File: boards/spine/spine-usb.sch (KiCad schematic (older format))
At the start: 34 parts, among them P1 USB_B, U1 93C56, U2 FT2232H, Y1 12 MHz

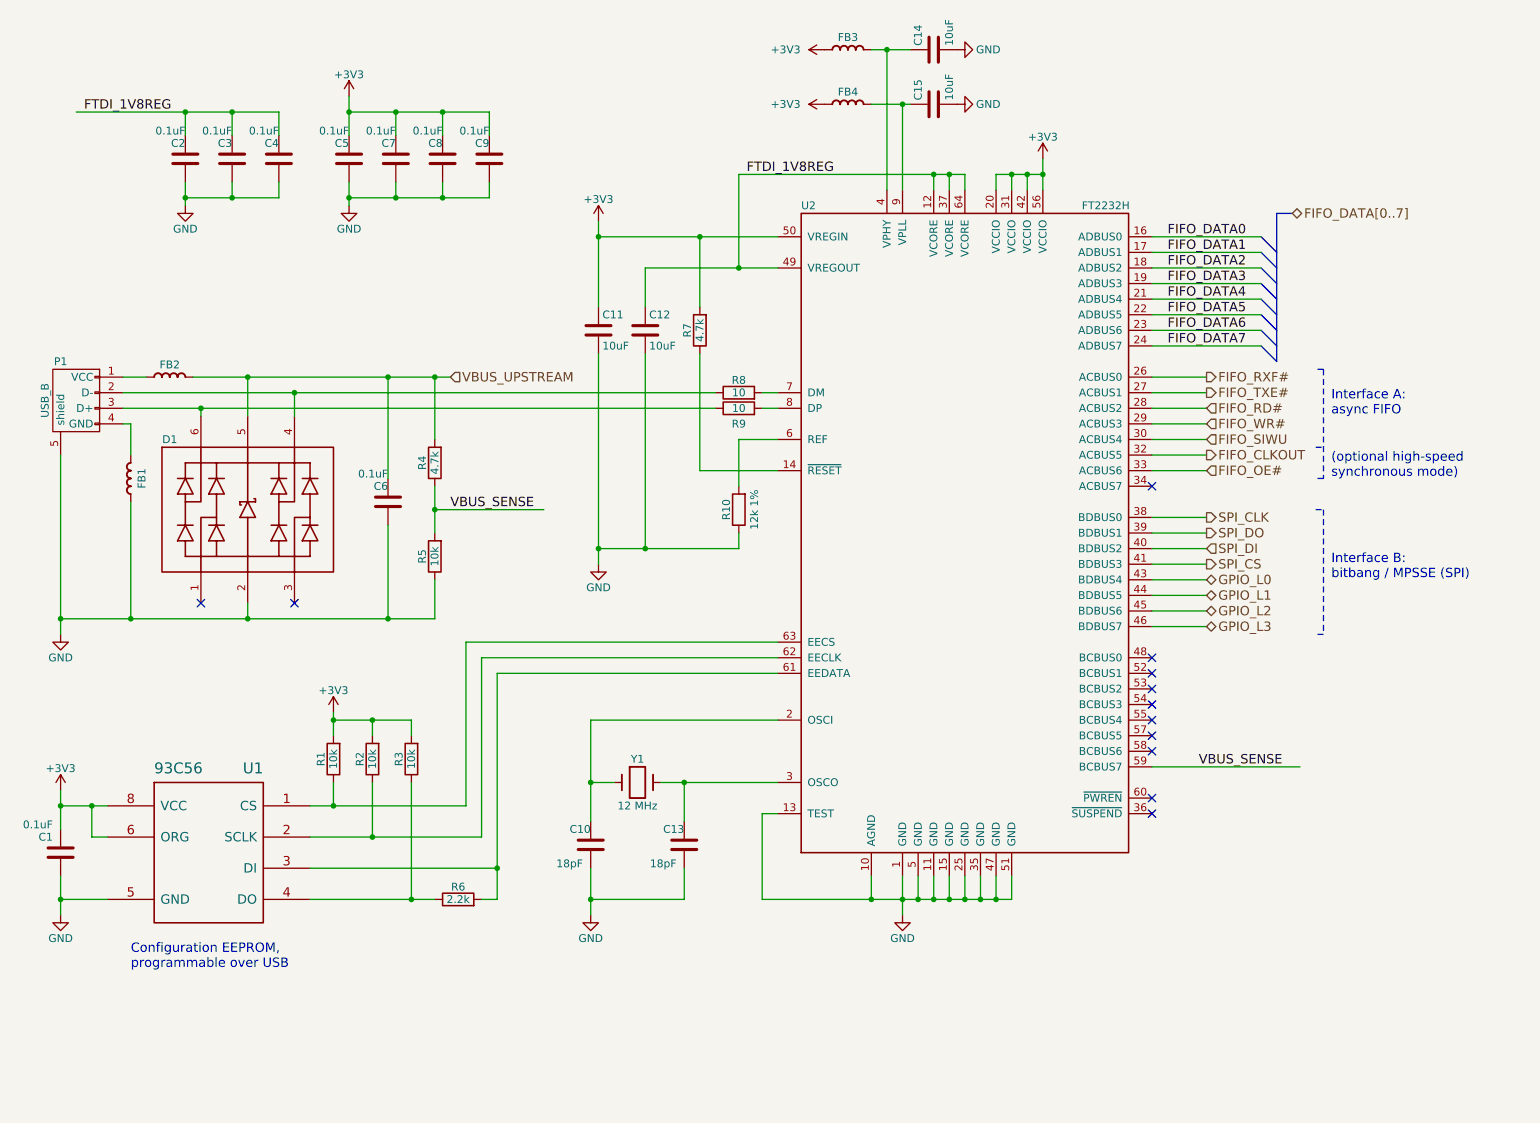
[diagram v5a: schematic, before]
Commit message: Pick better capacitors :)
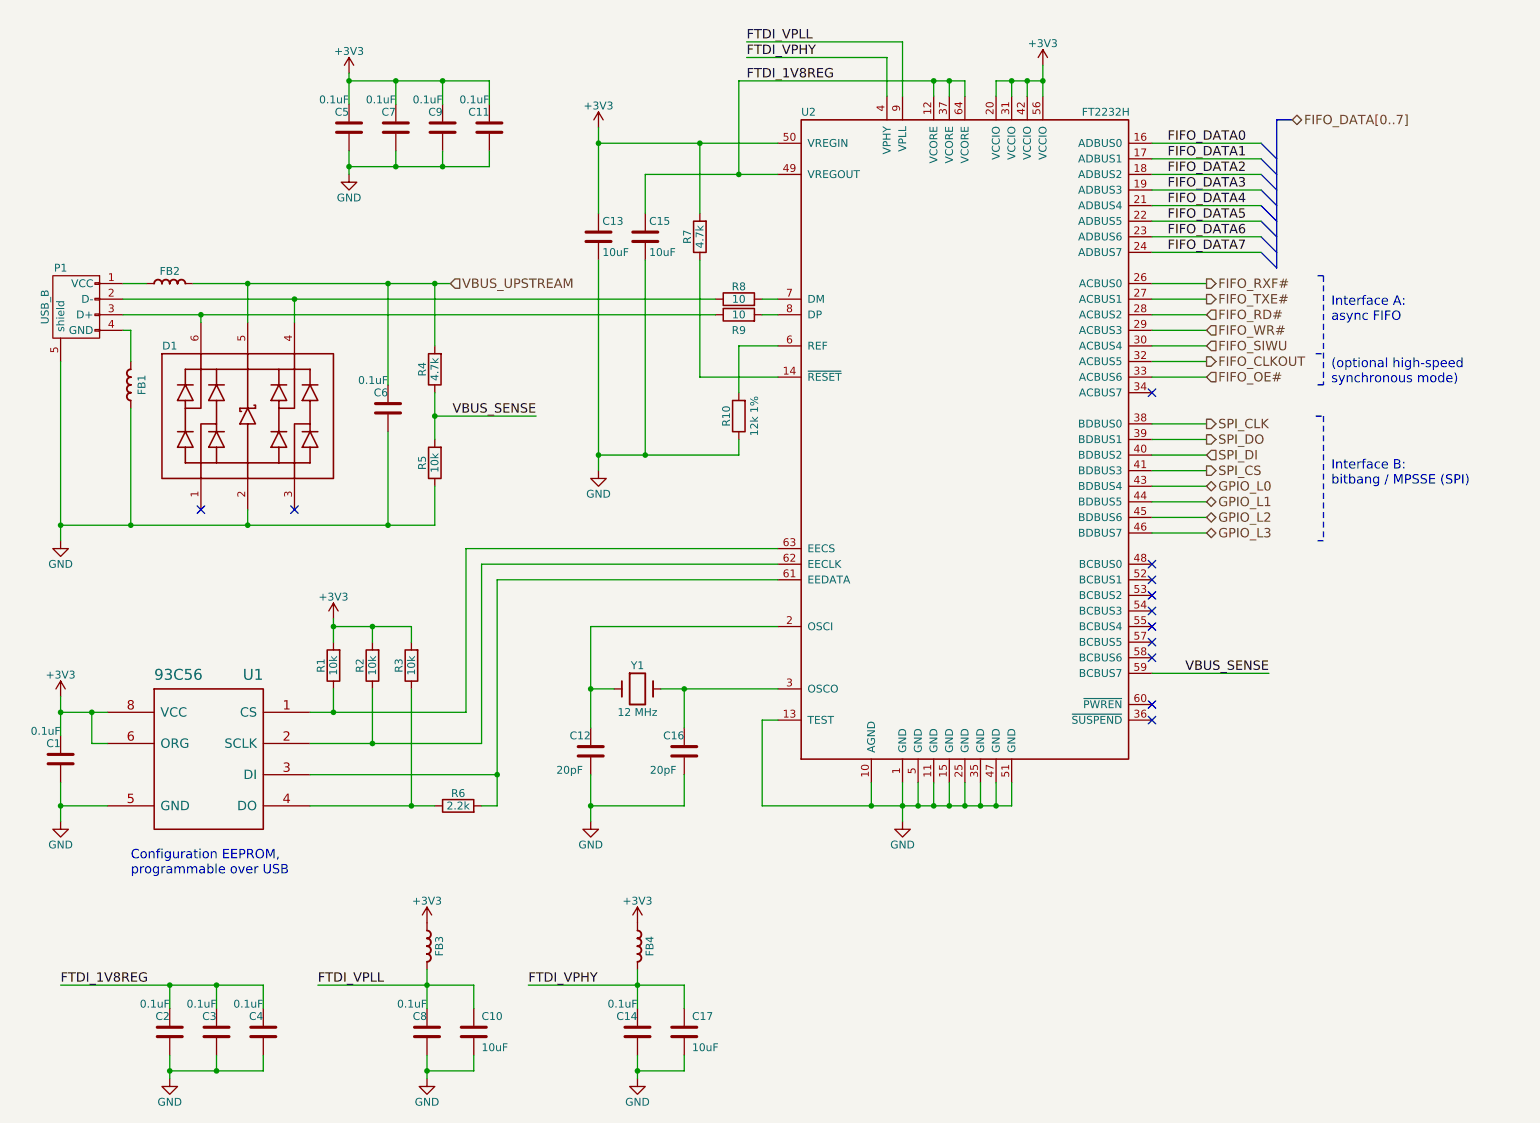
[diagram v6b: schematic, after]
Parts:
- removed C12: 10uF, symbol C
- removed C13: 18pF, symbol C
- removed FB3: Ferrite bead, symbol FERRITE_BEAD
- added C10, C17: 10uF, 1206, symbol C
- added C11: 0.1uF, 0805, symbol C
- added C16: 20pF, 0805, symbol C
- added FB4: Ferrite bead, symbol FERRITE_BEAD
- C1, C2, C3, C4, C5, C6, C7, C8, C9: footprint (none) -> 0805; MfgId CC0805ZRY5V9BB104 -> GRM21BR71H104MA01L; MfrId Yageo -> Murata; RefPrice1k 0.00783 -> 0.01880; Vend1Id 311-1361-1-ND -> 490-9672-2-ND
- C12: renamed from C10; value 18pF -> 20pF; footprint (none) -> 0805; MfgId CC0805JRNPO9BN180 -> CL21C200JBANNNC; MfrId Yageo -> Samsung; RefPrice1k 0.01266 -> 0.01485; Vend1Id 311-1102-1-ND -> 1276-1829-1-ND
- C13: renamed from C11; footprint (none) -> 1206; MfgId CC0805ZKY5V6BB106 -> GRM31CR61H106MA12L; MfrId Yageo -> Murata; RefPrice1k 0.03080 -> 0.07429; Vend1Id 311-1355-1-ND -> 490-10756-2-ND
- C14: value 10uF -> 0.1uF; footprint (none) -> 0805; MfgId CC0805ZKY5V6BB106 -> GRM21BR71H104MA01L; MfrId Yageo -> Murata; RefPrice1k 0.03080 -> 0.01880; Vend1Id 311-1355-1-ND -> 490-9672-2-ND
- C15: footprint (none) -> 1206; MfgId CC0805ZKY5V6BB106 -> GRM31CR61H106MA12L; MfrId Yageo -> Murata; RefPrice1k 0.03080 -> 0.07429; Vend1Id 311-1355-1-ND -> 490-10756-2-ND
- renumbered FB4 to FB3
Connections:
- net labels added: FTDI_VPHY, FTDI_VPLL
- wire segments 134 -> 146
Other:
- moved on the sheet: C12, C13, C2, D1, FB1, FB2, FB3, P1, R1, R10, R2, R3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

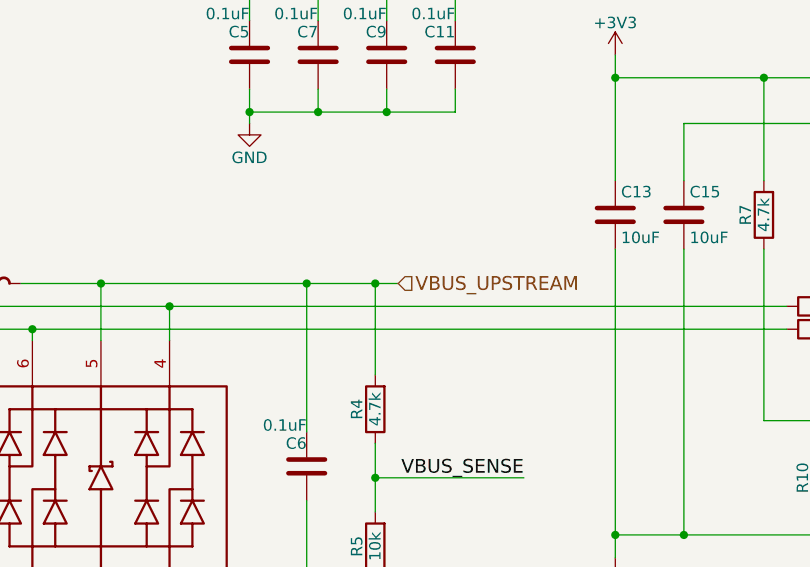
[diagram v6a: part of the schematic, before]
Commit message: Early power management work
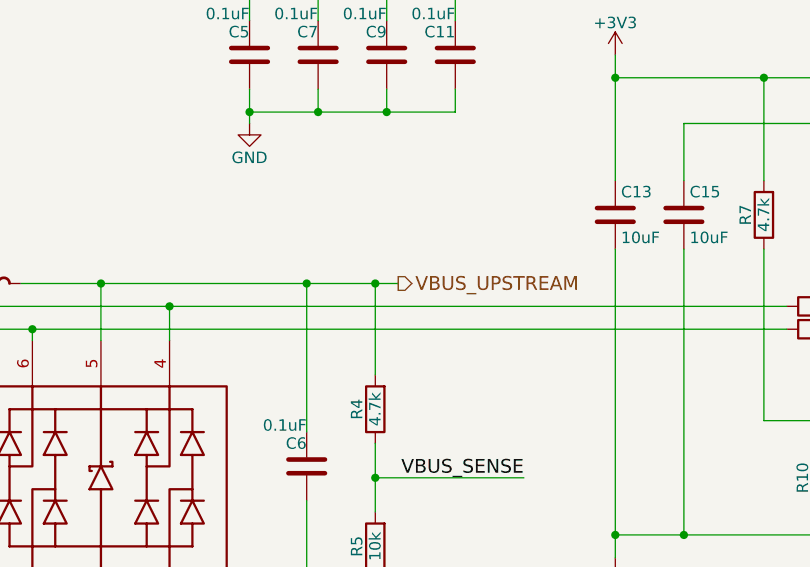
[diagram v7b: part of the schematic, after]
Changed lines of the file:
@@
 $Descr USLetter 11000 8500
 encoding utf-8
-Sheet 2 5
+Sheet 2 6
 Title ""
 Date ""
@@
 	1    0    0    -1
 $EndComp
-Text HLabel 3550 2350 2    60   Input ~ 0
+Text HLabel 3550 2350 2    60   Output ~ 0
 VBUS_UPSTREAM
 Text Label 4100 3200 2    60   ~ 0
@@
 $EndComp
 $Comp
-L GND #PWR01
+L GND #PWR1
 U 1 1 563F3C00
 P 1050 4000
-F 0 "#PWR01" H 1050 3750 50  0001 C CNN
+F 0 "#PWR1" H 1050 3750 50  0001 C CNN
 F 1 "GND" H 1050 3850 50  0000 C CNN
 F 2 "" H 1050 4000 60  0000 C CNN
@@
 $EndComp
 $Comp
-L +3V3 #PWR02
+L +3V3 #PWR11
 U 1 1 563F5B33
 P 4500 1350
-F 0 "#PWR02" H 4500 1200 50  0001 C CNN
+F 0 "#PWR11" H 4500 1200 50  0001 C CNN
 F 1 "+3V3" H 4500 1490 50  0000 C CNN
 F 2 "" H 4500 1350 60  0000 C CNN
@@
 NoConn ~ 1950 3800
 $Comp
-L GND #PWR03
+L GND #PWR12
 U 1 1 56407FC9
 P 4500 3550
-F 0 "#PWR03" H 4500 3300 50  0001 C CNN
+F 0 "#PWR12" H 4500 3300 50  0001 C CNN
 F 1 "GND" H 4500 3400 50  0000 C CNN
 F 2 "" H 4500 3550 60  0000 C CNN
@@
 $EndComp
 $Comp
-L +3V3 #PWR04
+L +3V3 #PWR16
 U 1 1 56409B2C
 P 7350 950
-F 0 "#PWR04" H 7350 800 50  0001 C CNN
+F 0 "#PWR16" H 7350 800 50  0001 C CNN
 F 1 "+3V3" H 7350 1090 50  0000 C CNN
 F 2 "" H 7350 950 60  0000 C CNN
@@
 $EndComp
 $Comp
-L +3V3 #PWR05
+L +3V3 #PWR2
 U 1 1 5640C498
 P 1050 5000
-F 0 "#PWR05" H 1050 4850 50  0001 C CNN
+F 0 "#PWR2" H 1050 4850 50  0001 C CNN
 F 1 "+3V3" H 1050 5140 50  0000 C CNN
 F 2 "" H 1050 5000 60  0000 C CNN
@@
 $EndComp
 $Comp
-L GND #PWR06
+L GND #PWR3
 U 1 1 5640C700
 P 1050 5800
-F 0 "#PWR06" H 1050 5550 50  0001 C CNN
+F 0 "#PWR3" H 1050 5550 50  0001 C CNN
 F 1 "GND" H 1050 5650 50  0000 C CNN
 F 2 "" H 1050 5800 60  0000 C CNN
@@
 $EndComp
 $Comp
-L +3V3 #PWR07
+L +3V3 #PWR5
 U 1 1 5640CB0D
 P 2800 4500
-F 0 "#PWR07" H 2800 4350 50  0001 C CNN
+F 0 "#PWR5" H 2800 4350 50  0001 C CNN
 F 1 "+3V3" H 2800 4640 50  0000 C CNN
 F 2 "" H 2800 4500 60  0000 C CNN
@@
 $EndComp
 $Comp
-L GND #PWR08
+L GND #PWR4
 U 1 1 5640EC58
 P 1750 7450
-F 0 "#PWR08" H 1750 7200 50  0001 C CNN
+F 0 "#PWR4" H 1750 7200 50  0001 C CNN
 F 1 "GND" H 1750 7300 50  0000 C CNN
 F 2 "" H 1750 7450 60  0000 C CNN
@@
 $EndComp
 $Comp
-L GND #PWR09
+L GND #PWR7
 U 1 1 5640ECEA
 P 2900 1650
-F 0 "#PWR09" H 2900 1400 50  0001 C CNN
+F 0 "#PWR7" H 2900 1400 50  0001 C CNN
 F 1 "GND" H 2900 1500 50  0000 C CNN
 F 2 "" H 2900 1650 60  0000 C CNN
@@
 FTDI_1V8REG
 $Comp
-L +3V3 #PWR010
+L +3V3 #PWR6
 U 1 1 5640F443
 P 2900 1000
-F 0 "#PWR010" H 2900 850 50  0001 C CNN
+F 0 "#PWR6" H 2900 850 50  0001 C CNN
 F 1 "+3V3" H 2900 1140 50  0000 C CNN
 F 2 "" H 2900 1000 60  0000 C CNN
@@
 $EndComp
 $Comp
-L GND #PWR011
+L GND #PWR10
 U 1 1 56411C34
 P 4450 5800
-F 0 "#PWR011" H 4450 5550 50  0001 C CNN
+F 0 "#PWR10" H 4450 5550 50  0001 C CNN
 F 1 "GND" H 4450 5650 50  0000 C CNN
 F 2 "" H 4450 5800 60  0000 C CNN
@@
 $EndComp
 $Comp
-L GND #PWR012
+L GND #PWR15
 U 1 1 56412014
 P 6450 5800
-F 0 "#PWR012" H 6450 5550 50  0001 C CNN
+F 0 "#PWR15" H 6450 5550 50  0001 C CNN
 F 1 "GND" H 6450 5650 50  0000 C CNN
 F 2 "" H 6450 5800 60  0000 C CNN
@@
 $EndComp
 $Comp
-L GND #PWR013
+L GND #PWR9
 U 1 1 5642A93B
 P 3400 7450
-F 0 "#PWR013" H 3400 7200 50  0001 C CNN
+F 0 "#PWR9" H 3400 7200 50  0001 C CNN
 F 1 "GND" H 3400 7300 50  0000 C CNN
 F 2 "" H 3400 7450 60  0000 C CNN
@@
 	3700 7400 3700 7300
 $Comp
-L +3V3 #PWR014
+L +3V3 #PWR8
 U 1 1 5642B955
 P 3400 6450
-F 0 "#PWR014" H 3400 6300 50  0001 C CNN
+F 0 "#PWR8" H 3400 6300 50  0001 C CNN
 F 1 "+3V3" H 3400 6590 50  0000 C CNN
 F 2 "" H 3400 6450 60  0000 C CNN
@@
 $EndComp
 $Comp
-L GND #PWR015
+L GND #PWR14
 U 1 1 5642BC5C
 P 4750 7450
-F 0 "#PWR015" H 4750 7200 50  0001 C CNN
+F 0 "#PWR14" H 4750 7200 50  0001 C CNN
 F 1 "GND" H 4750 7300 50  0000 C CNN
 F 2 "" H 4750 7450 60  0000 C CNN
@@
 	5050 7400 5050 7300
 $Comp
-L +3V3 #PWR016
+L +3V3 #PWR13
 U 1 1 5642BC76
 P 4750 6450
-F 0 "#PWR016" H 4750 6300 50  0001 C CNN
+F 0 "#PWR13" H 4750 6300 50  0001 C CNN
 F 1 "+3V3" H 4750 6590 50  0000 C CNN
 F 2 "" H 4750 6450 60  0000 C CNN
